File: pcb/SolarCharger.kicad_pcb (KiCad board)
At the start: 4 copper layers, 24.1 x 30.8 mm, 37 parts, among them J1 Conn_01x02_Pin, J2 Conn_01x02_Pin, J3 Conn_01x02_Pin, Q1 PMOS, U1 BQ24074, U2 M3406-ADJ

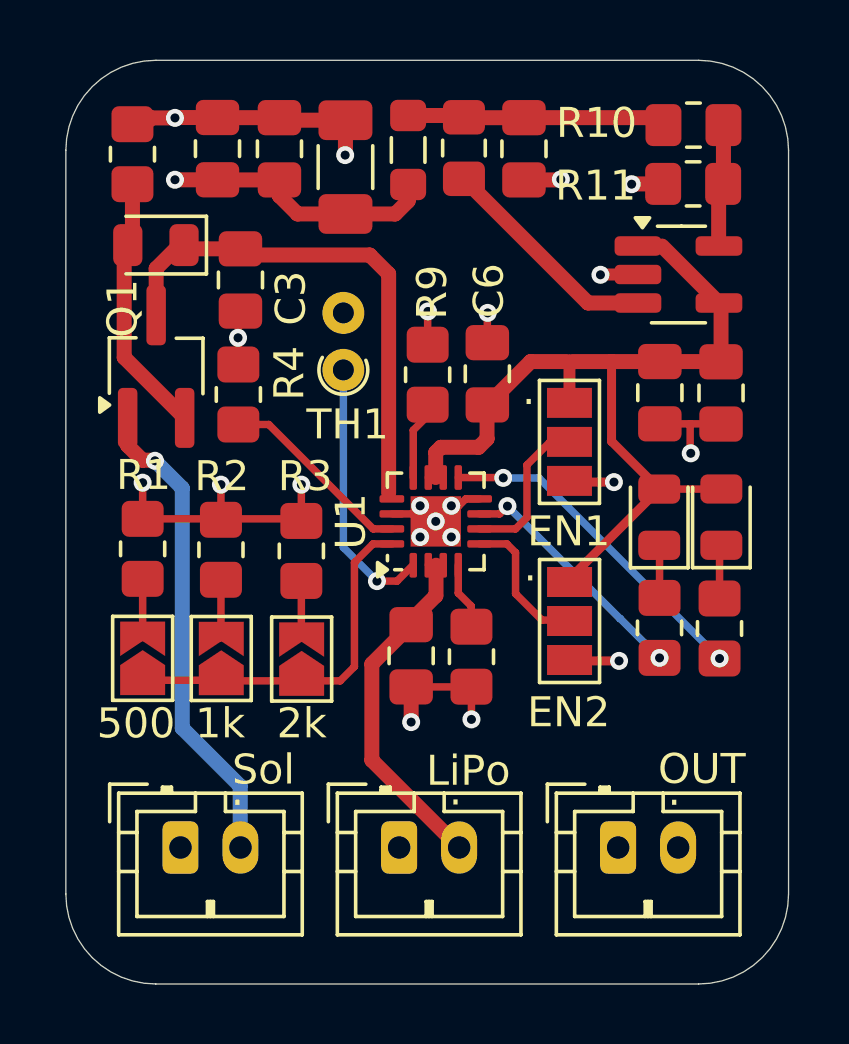
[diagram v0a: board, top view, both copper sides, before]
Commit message: pcb: smaller eyecandy stuff. No functional changes.
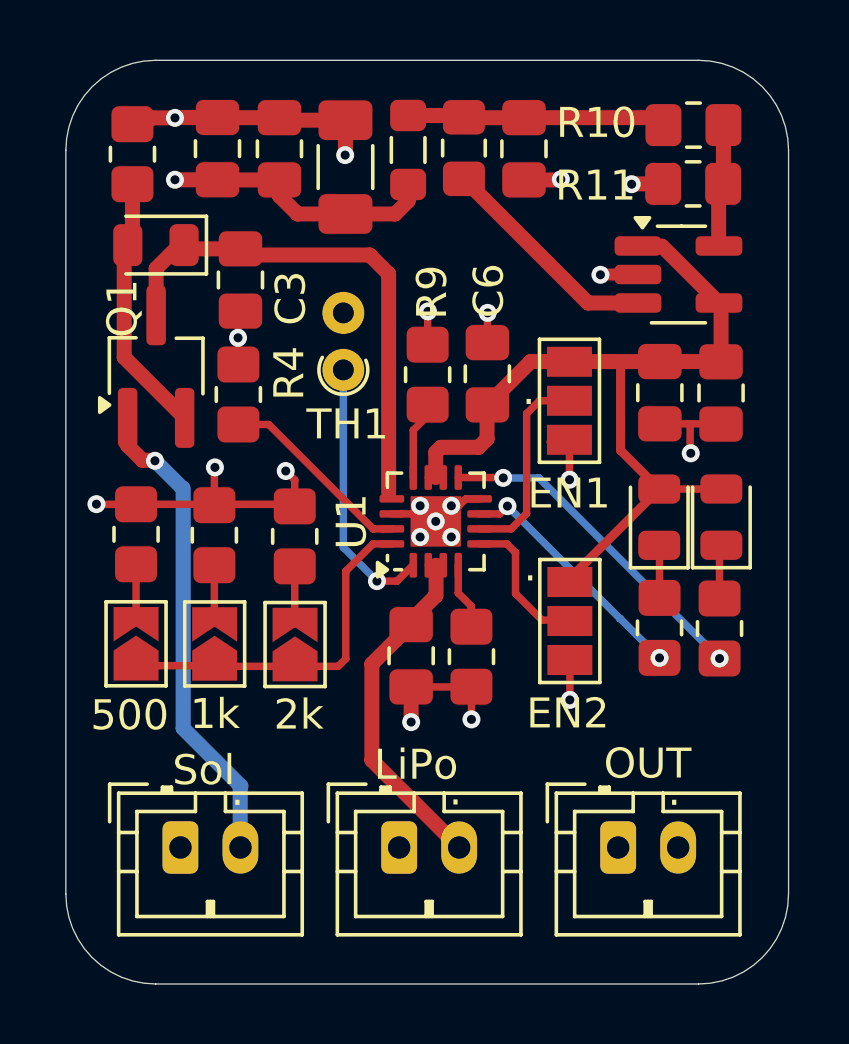
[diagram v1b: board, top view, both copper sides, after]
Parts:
- moved JP4 1.37 mm to (115.7, 81.6)
- moved JP1 0.53 mm to (101.2, 89.7)
- moved JP2 0.53 mm to (103.8, 89.7)
- moved JP3 0.53 mm to (106.5, 89.7)
- moved R1 0.53 mm to (101.2, 86.0)
- moved R2 0.53 mm to (103.8, 86.0)
- moved R3 0.53 mm to (106.5, 86.1)
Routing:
- net Net-(JP4-C): track 5.23 -> 6.71 mm
- net /OUT: track 30.5 -> 29.3 mm
- net GND: track 36.5 -> 37.3 mm

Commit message: pcb: eyecandy stuff destoryed the solderbridge marker
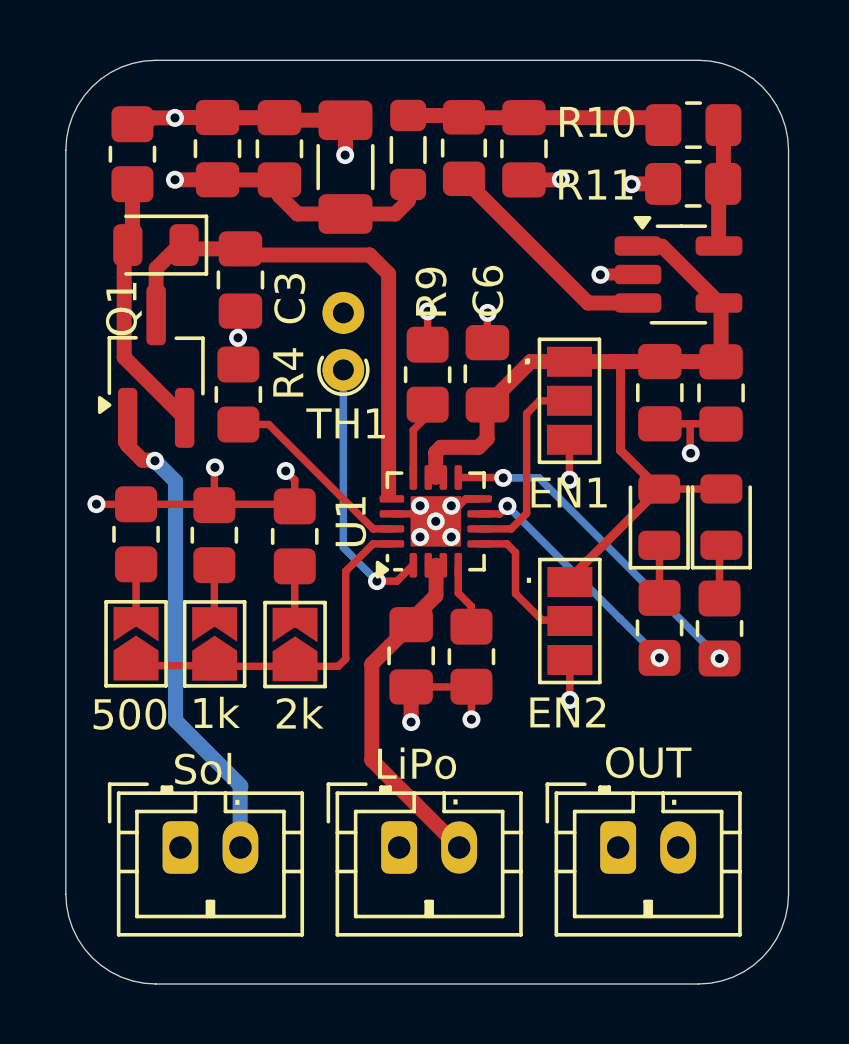
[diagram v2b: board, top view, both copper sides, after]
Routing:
- net GND: track 37.3 -> 36.2 mm
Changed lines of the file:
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@@
+		)
+	)
+	(gr_text "."
+		(at 114.08 80.44 0)
+		(layer "F.SilkS")
+		(effects
+			(font
+				(size 1 1)
+				(thickness 0.15)
+			)
+			(justify left bottom)
 		)
 	)
@@
 	)
 	(gr_text "."
-		(at 114.15 87.67 0)
+		(at 114.11 87.75 0)
+		(layer "F.SilkS")
+		(effects
+			(font
+				(size 1 1)
+				(thickness 0.15)
+			)
+			(justify left bottom)
+		)
+	)
+	(gr_text "."
+		(at 114.04 80.47 0)
 		(layer "F.SilkS")
 		(effects
@@
 		)
 	)
-	(gr_text "."
-		(at 114.1 81.79 0)
-		(layer "F.SilkS")
-		(effects
-			(font
-				(size 1 1)
-				(thickness 0.15)
-			)
-			(justify left bottom)
-		)
-	)
 	(gr_text "LiPo"
 		(at 109.16 94.28 0)
@@
 	)
 	(segment
-		(start 115.6775 80.3375)
-		(end 115.7625 80.2525)
-		(width 0.4)
-		(layer "F.Cu")
-		(net 1)
-	)
-	(segment
 		(start 112.65 83.11)
 		(end 112.93 82.83)
@@
 	)
 	(segment
-		(start 115.6775 80.3375)
-		(end 115.5925 80.2525)
-		(width 0.4)
-		(layer "F.Cu")
-		(net 1)
-	)
-	(segment
 		(start 111.39 83.11)
 		(end 111.22 83.28)
@@
 	)
 	(segment
-		(start 115.03 82.93)
-		(end 115.6775 82.93)
-		(width 0.25)
-		(layer "F.Cu")
-		(net 2)
-	)
-	(segment
 		(start 106.01 72.1225)
 		(end 103.95 72.1225)
@@
 		(end 106.52 84.2)
 		(width 0.25)
-		(layer "F.Cu")
-		(net 2)
-	)
-	(segment
-		(start 101.11 72.34)
-		(end 101.53 72.34)
-		(width 0.5)
 		(layer "F.Cu")
 		(net 2)
@@
 	)
 	(segment
-		(start 102.865 76.495)
-		(end 102.71 76.34)
-		(width 0.5)
-		(layer "F.Cu")
-		(net 4)
-	)
-	(segment
 		(start 109.02 76.7)
 		(end 109.65 77.33)
@@
 	)
 	(segment
-		(start 118.5625 72.1225)
-		(end 118.81 72.37)
-		(width 0.5)
-		(layer "F.Cu")
-		(net 5)
-	)
-	(segment
 		(start 114.16 72.1225)
 		(end 118.5625 72.1225)
@@
 	)
 	(segment
-		(start 101.11 76.065)
-		(end 100.835 76.34)
-		(width 0.5)
-		(layer "F.Cu")
-		(net 23)
-	)
-	(segment
 		(start 101.84 83.54)
 		(end 101.44 83.54)
@@
 	)
 	(segment
+		(start 102.55 84.25)
+		(end 101.86 83.56)
+		(width 0.5)
+		(layer "B.Cu")
+		(net 24)
+	)
+	(segment
 		(start 104.7 94.4)
 		(end 104.7 96.45)
@@
 	)
 	(segment
-		(start 102.8 92.475)
-		(end 104.73 94.405)
+		(start 104.73 94.405)
+		(end 102.55 92.225)
 		(width 0.5)
 		(layer "B.Cu")
@@
 	)
 	(segment
-		(start 102.8 84.475)
-		(end 102.8 92.475)
+		(start 102.55 92.225)
+		(end 102.55 84.25)
 		(width 0.5)
 		(layer "B.Cu")
-		(net 24)
-	)
-	(segment
-		(start 101.86 83.56)
-		(end 102.77 84.47)
-		(width 0.5)
-		(layer "B.Cu")

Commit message: pcb, schematic: get rid of non-standard p-mosfet and replace it with an AO3401
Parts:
- Q1: value PMOS -> AO3401A; footprint Package_TO_SOT_SMD:TSOT-23_HandSoldering -> Package_TO_SOT_SMD:SOT-23
- moved Q1 0.89 mm to (101.8, 79.5)
- moved R4 0.07 mm to (104.7, 81.4)
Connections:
- Q1 pad 1: Net-(J2-Pin_2) -> Net-(D3-A)
- Q1 pad 2: Net-(D3-A) -> /VBUS
- Q1 pad 3: /VBUS -> Net-(J2-Pin_2)
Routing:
- net Net-(J2-Pin_2): track 16.1 -> 19.1 mm
- net Net-(D3-A): track 8.35 -> 5.77 mm
- net /VBUS: track 16.6 -> 18.0 mm
